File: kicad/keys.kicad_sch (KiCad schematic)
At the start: 1 part, among them J1 Conn_01x03

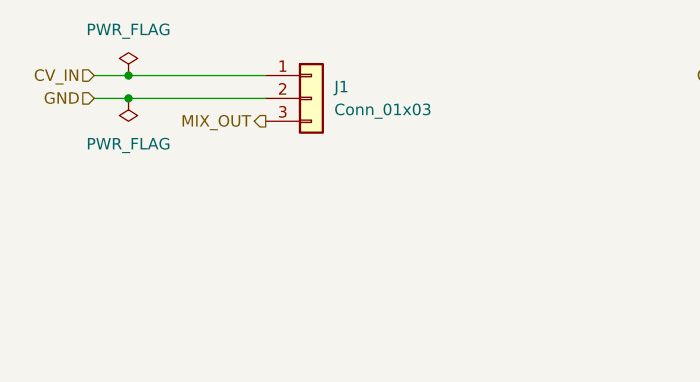
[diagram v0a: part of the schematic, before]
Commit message: mark components as DNP, add LCSC part numbers
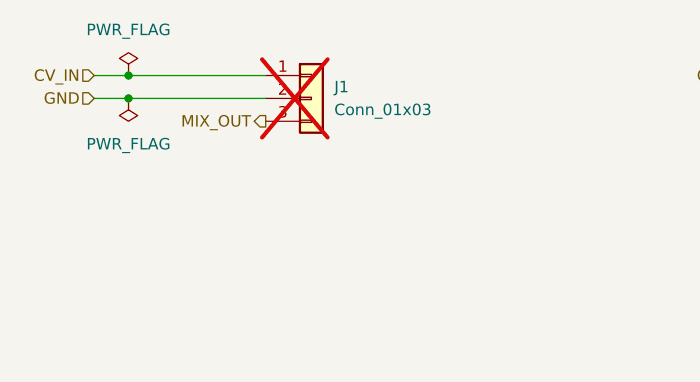
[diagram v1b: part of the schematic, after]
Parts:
- J1: now not fitted
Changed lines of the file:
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@@
 		(in_bom yes)
 		(on_board yes)
-		(dnp no)
+		(dnp yes)
 		(fields_autoplaced yes)
 		(property "Reference" "J1"
@@
 			(at 59.69 55.88 0)
 			(effects
+				(font
+					(size 1.27 1.27)
+				)
+				(hide yes)
+			)
+		)
+		(property "LCSC Part" ""
+			(at 59.69 55.88 0)
+			(effects
